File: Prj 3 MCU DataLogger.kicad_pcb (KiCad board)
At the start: 2 copper layers, 29 parts, among them J1 Conn_01x04_Male, J2 Conn_01x04_Male, J3 Conn_01x09_Male, J4 Conn_02x03_Odd_Even, U1 24LC1025, U2 24LC1025, U3 DS1337S_, U4 ATMEGA328P-AU, Y1 16 MHz, Y2 32.768 KHz

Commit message: Complete footprint placements.
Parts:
- moved H1 161.8 mm to (90.1, 73.6)
- moved H2 157.3 mm to (90.2, 99.4)
- moved BT1 157.2 mm to (90.9, 82.7)
- moved R1 146.1 mm to (97.3, 95.6)
- moved R2 139.9 mm to (103.1, 95.9), turned to 0 degrees
- moved U2 136.4 mm to (101.0, 78.5)
- moved U1 135.8 mm to (101.5, 85.7)
- moved Y2 134.9 mm to (90.8, 90.5), turned to 90 degrees
- moved U3 132.5 mm to (102.6, 91.8), turned to 0 degrees
- moved R3 123.0 mm to (121.6, 83.3)
- moved C1 122.9 mm to (105.6, 73.2)
- moved R6 122.3 mm to (121.6, 78.5)
- moved U4 121.3 mm to (113.0, 82.4), turned to 0 degrees
- moved J3 120.3 mm to (94.9, 99.7), turned to 90 degrees
- moved R5 117.5 mm to (126.3, 82.7)
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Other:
- board outline added: 50.8 x 30.5 mm

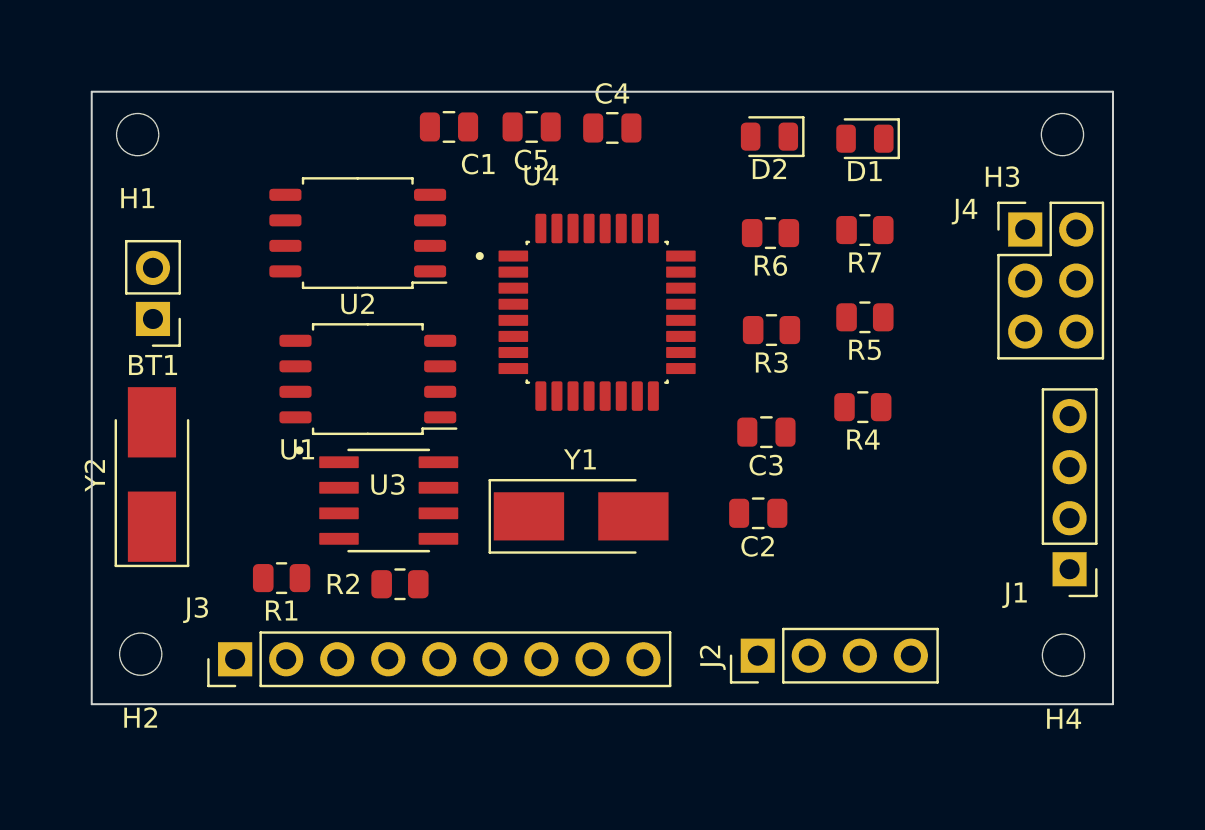
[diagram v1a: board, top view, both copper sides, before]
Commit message: Routings have been completed except Vcc & GND Copper filled zones.
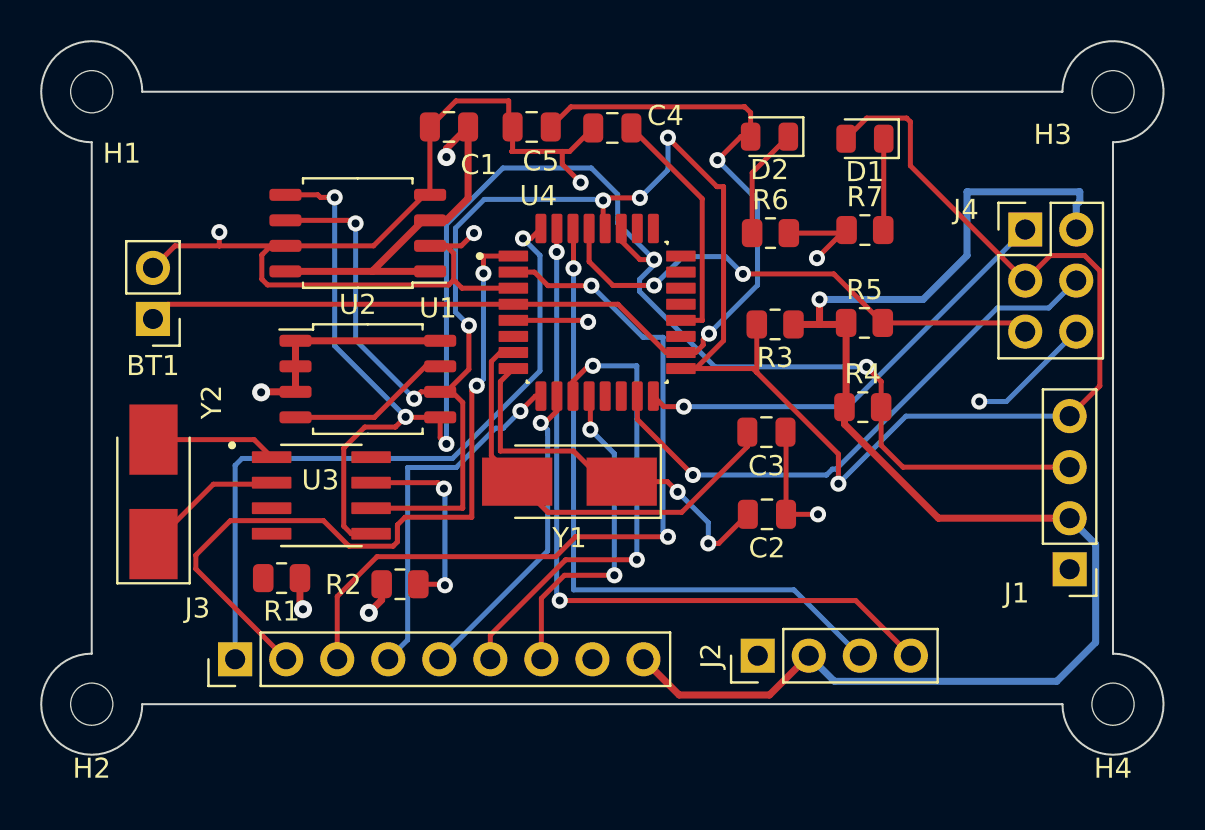
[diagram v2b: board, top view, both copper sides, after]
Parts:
- moved H2 3.48 mm to (87.8, 101.9)
- moved H4 3.47 mm to (138.6, 101.9)
- moved U3 3.36 mm to (99.2, 91.5)
- moved H3 3.30 mm to (138.6, 71.4)
- moved H1 3.13 mm to (87.8, 71.4)
- moved Y1 1.82 mm to (111.6, 90.8), turned to 180 degrees
- moved Y2 0.87 mm to (90.9, 91.3)
- moved C2 0.44 mm to (121.4, 92.5)
- moved R3 0.33 mm to (121.8, 83.0)
- moved R5 0.28 mm to (126.3, 82.9), turned to 0 degrees
- turned R4 to 0 degrees
- turned R6 to 0 degrees
- turned R7 to 0 degrees
- turned U1 to 0 degrees
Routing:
- net /SCK: track 0.00 -> 117.0 mm, vias 0 -> 7
- net /Vcc: track 0.00 -> 107.1 mm, vias 0 -> 5
- net /SDA: track 0.00 -> 83.7 mm, vias 0 -> 5
- net GND: track 0.00 -> 82.6 mm, vias 0 -> 7
- net Net-(BT1-+): track 0.00 -> 53.8 mm, vias 0 -> 2
- net /D4: track 0.00 -> 39.6 mm, vias 0 -> 2
- net /D3: track 0.00 -> 37.8 mm, vias 0 -> 2
- net /TX: track 0.00 -> 37.2 mm, vias 0 -> 2
- net /D2: track 0.00 -> 34.8 mm, vias 0 -> 1
- net /RX: track 0.00 -> 33.6 mm, vias 0 -> 1
- net /MOSI: track 0.00 -> 28.2 mm, vias 0 -> 1
- net /RESET: track 0.00 -> 26.0 mm, vias 0 -> 2
- net /D7: track 0.00 -> 23.9 mm, vias 0 -> 2
- net /MISO: track 0.00 -> 22.4 mm, vias 0 -> 1
- net Net-(U4-PB6): track 0.00 -> 22.0 mm
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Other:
- board size 50.8 x 30.5 mm -> 55.9 x 35.5 mm

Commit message: Fixed all DRC errors and F&B Silkscreens completed.
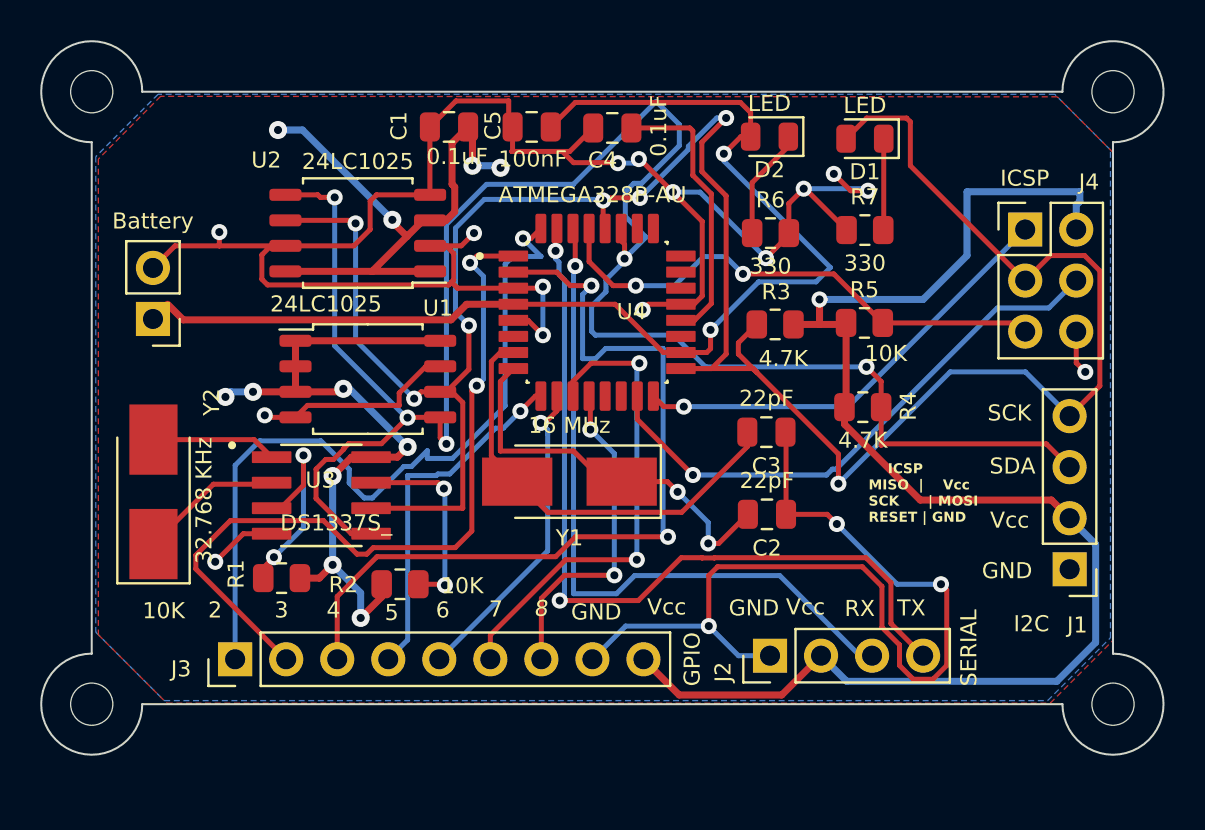
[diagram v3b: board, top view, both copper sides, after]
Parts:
- added REF**: KiCad-Logo2_5mm_SilkScreen, Symbol:KiCad-Logo2_5mm_SilkScreen, B.Cu at (99.4, 81.6)
- moved J2 0.61 mm to (121.6, 99.5)
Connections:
- BT1 pad 1: Net-(BT1-+) -> /Vcc
- C5 pad 1: Net-(BT1-+) -> /Vcc
- D2 pad 2: Net-(BT1-+) -> /Vcc
- U4 pad 18: Net-(BT1-+) -> /Vcc
- U4 pad 4: Net-(BT1-+) -> /Vcc
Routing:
- net /Vcc: track 107.1 -> 198.1 mm, vias 5 -> 14
- net GND: track 82.6 -> 156.7 mm, vias 7 -> 18
- net Net-(BT1-+): track 53.8 -> 0.00 mm, vias 2 -> 0
- net /SDA: track 83.7 -> 97.4 mm
- net Net-(U3-~{INTA}): track 0.00 -> 10.5 mm, vias 0 -> 2
- net /SCK: track 117.0 -> 123.2 mm
- net /D2: track 34.8 -> 39.0 mm
- net /TX: track 37.2 -> 41.0 mm
- net /D4: track 39.6 -> 42.5 mm
- net Net-(U4-AREF): track 12.1 -> 13.9 mm
- net /RX: track 33.6 -> 35.3 mm
- net /D3: track 37.8 -> 38.8 mm
- added copper zone on F.Cu, net /Vcc
- added copper zone on B.Cu, net GND
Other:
- board text added: "- 2Mbit EEPROM - RTC - I2C , SPI , GPIOs"
- board text added: "2"
- board text added: "3"
- board text added: "4"
- board text added: "5"
- board text added: "6"
- board text added: "7"
- board text added: "8"
- board text added: "Data Logger with the ATMega328P."
- board text added: "GND"
- board text added: "GPIO"
- board text added: "I2C"
- board text added: "ICSP"
- board text added: "ICSP MISO | Vcc SCK | MOSI RESET | GND"
- board text added: "RX"
- board text added: "SCK"
- board text added: "SDA"
- board text added: "SERIAL"
- board text added: "TX"
- board text added: "Vcc"

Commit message: MCU Datalogger with 2 layers Project is completed & Gerbers are imported ; ready for manufacturing.
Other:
- board text added: "+"
- board text added: "-"
- board text added: "0.2000 mm / 0.0000 mm"
- board text added: "0.3000 mm"
- board text added: "1.6000 mm"
- board text added: "55.8612 mm x 35.5158 mm"
- board text added: "BOARD CHARACTERISTICS"
- board text added: "Board Thickness:"
- board text added: "Board overall dimensions:"
- board text added: "Castellated pads:"
- board text added: "Copper Finish:"
- board text added: "Copper Layer Count:"
- board text added: "Edge card connectors:"
- board text added: "Impedance Control:"
- board text added: "Min hole diameter:"
- board text added: "Min track/spacing:"
- board text added: "No"
- board text added: "None"
- board text added: "Plated Board Edge:"
